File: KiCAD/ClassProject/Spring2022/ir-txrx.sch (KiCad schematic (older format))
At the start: 1 part

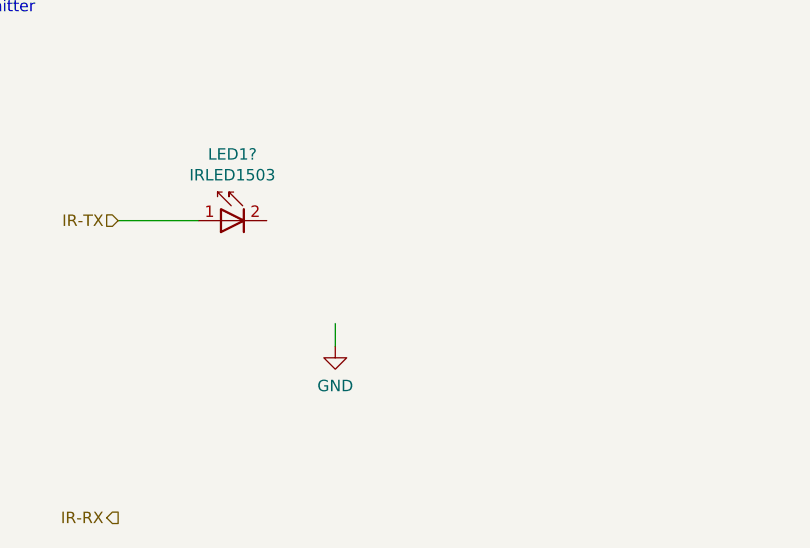
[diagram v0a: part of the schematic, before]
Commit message: Added decoupling caps and pull up resistors from PONTECH library
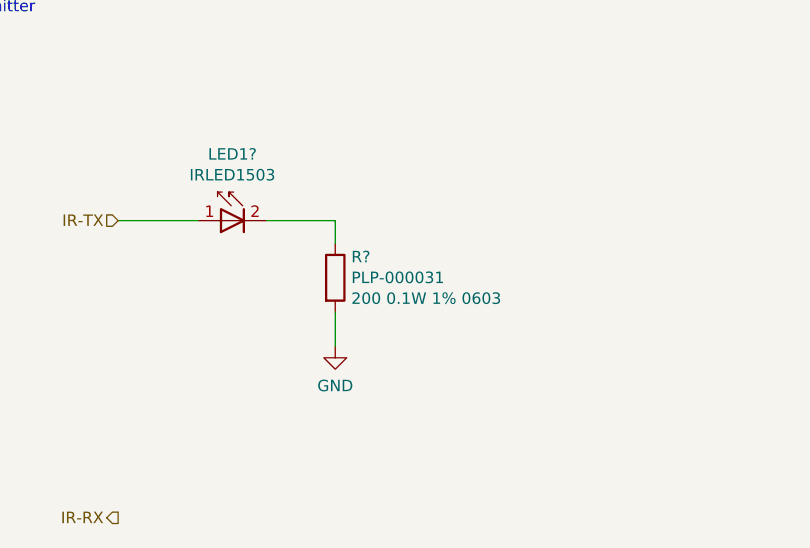
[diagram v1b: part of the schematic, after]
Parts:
- added R?: PLP-000031, a_pontech:R_0603_1608Metric, symbol 1_pontech:PLP-000031
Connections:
- wire segments 2 -> 4
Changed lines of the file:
@@
 Wire Wire Line
 	1900 2000 2250 2000
-Wire Wire Line
-	2850 2450 2850 2550
 $Comp
 L 74_Jacob:GND #PWR?
@@
 	1    0    0    -1
 $EndComp
+$Comp
+L 1_pontech:PLP-000031 R?
+U 1 1 62644FF5
+P 2850 2250
+F 0 "R?" H 2920 2341 50  0000 L CNN
+F 1 "PLP-000031" H 2920 2250 50  0000 L CNN
+F 2 "a_pontech:R_0603_1608Metric" V 2780 2250 50  0001 C CNN
+F 3 "~" H 2850 2250 50  0001 C CNN
+F 4 "200 0.1W 1% 0603" H 2920 2159 50  0000 L CNN "Info"
+	1    2850 2250
+	1    0    0    -1
+$EndComp
+Wire Wire Line
+	2850 2400 2850 2550
+Wire Wire Line
+	2850 2100 2850 2000
+Wire Wire Line
+	2850 2000 2550 2000
 $EndSCHEMATC

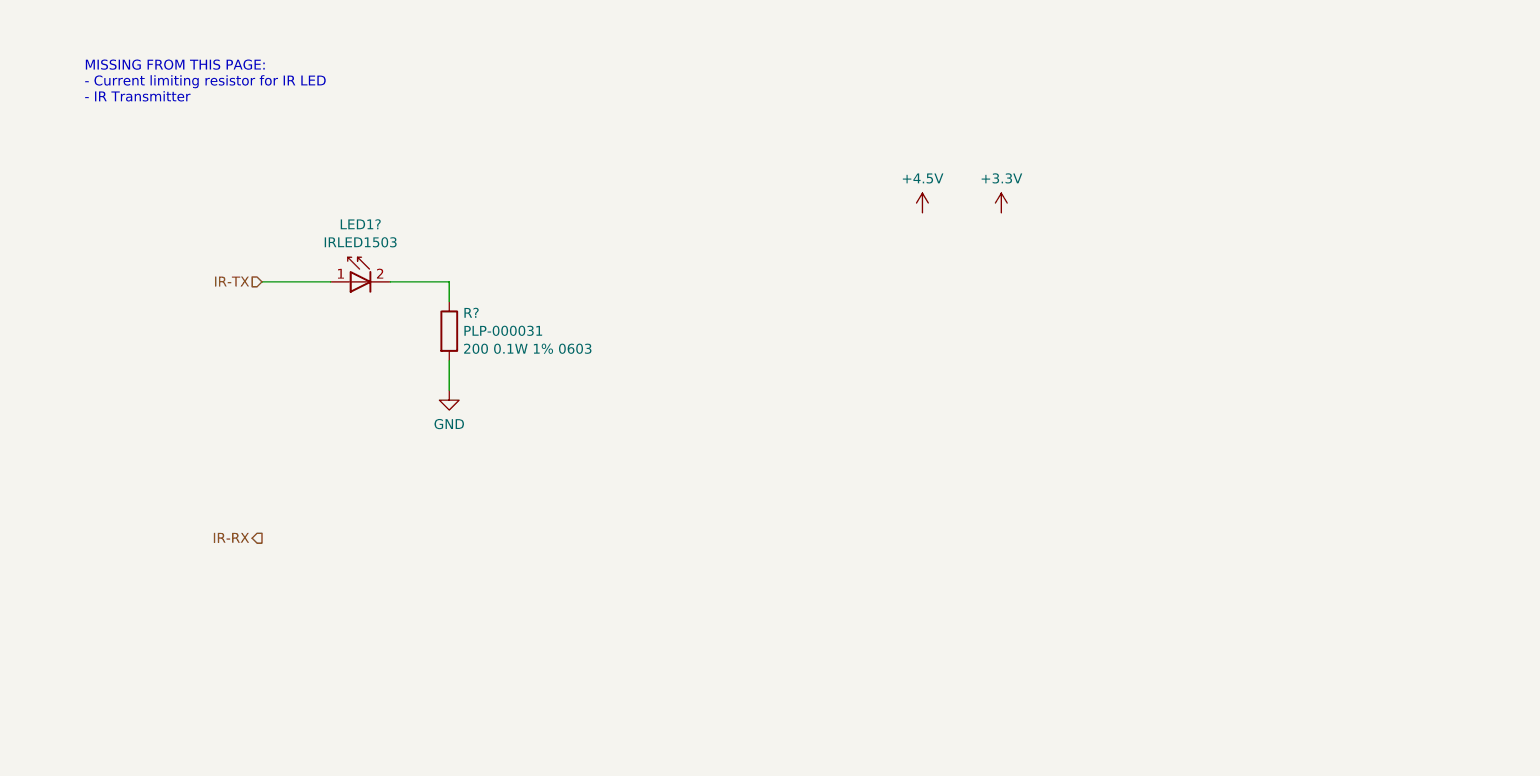
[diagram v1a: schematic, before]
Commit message: Added IR Tx
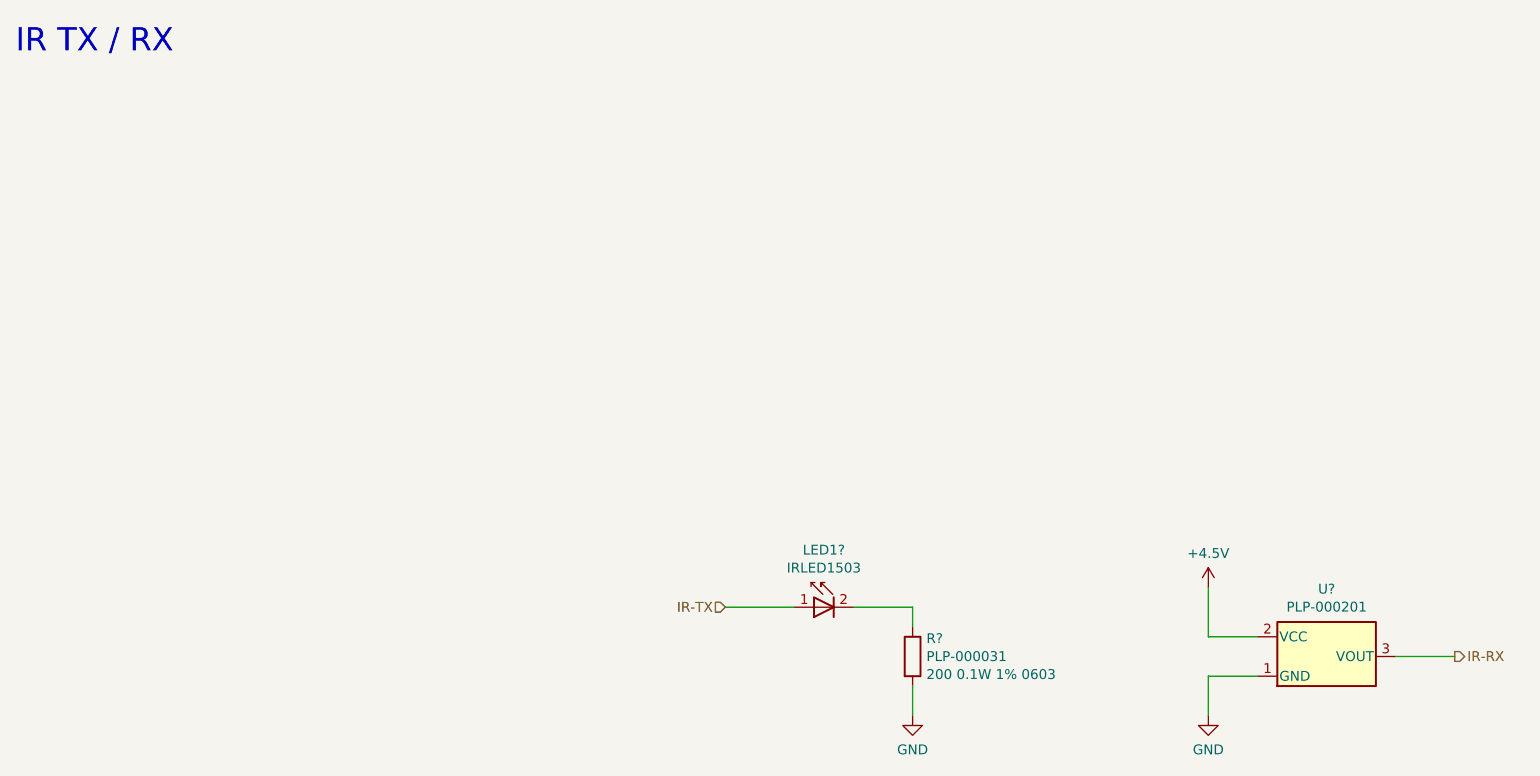
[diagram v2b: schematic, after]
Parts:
- added U?: PLP-000201, 1_pontech:PLP-0000201, symbol 1_pontech:PLP-000201
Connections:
- net +4V: now also U?.2 (VCC)
- net GND: now also U?.1 (GND)
- net IR-RX: now also U?.3 (VOUT)
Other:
- note added: "IR TX / RX"
- note removed: "MISSING FROM THIS PAGE:\n- Current limiting resistor for IR LED\n- IR Transmitter"
- moved on the sheet: LED1?, R?
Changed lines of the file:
@@
 L 74_Jordan_IRSchematic:IRLED1503 LED1?
 U 1 1 6265B928
-P 2400 2000
-F 0 "LED1?" H 2400 2290 50  0000 C CNN
-F 1 "IRLED1503" H 2400 2199 50  0000 C CNN
-F 2 "74_ClassProj_IRFootprint:IR1503" H 2400 1825 50  0001 C CNN
-F 3 "http://www.alliedelec.com/m/d/40788c34903a719969df15f1fbea1056.pdf" H 2750 1750 50  0001 C CNN
-	1    2400 2000
+P 4750 3650
+F 0 "LED1?" H 4750 3940 50  0000 C CNN
+F 1 "IRLED1503" H 4750 3849 50  0000 C CNN
+F 2 "74_ClassProj_IRFootprint:IR1503" H 4750 3475 50  0001 C CNN
+F 3 "http://www.alliedelec.com/m/d/40788c34903a719969df15f1fbea1056.pdf" H 5100 3400 50  0001 C CNN
+	1    4750 3650
 	-1   0    0    -1
 $EndComp
-Text Notes 1000 1100 0    50   ~ 0
-MISSING FROM THIS PAGE:\n- Current limiting resistor for IR LED\n- IR Transmitter
-Text HLabel 1900 2000 0    50   Input ~ 0
+Text HLabel 4250 3650 0    50   Input ~ 0
 IR-TX
-Text HLabel 1900 3300 0    50   Output ~ 0
+Text HLabel 7950 3900 2    50   Output ~ 0
 IR-RX
 Wire Wire Line
-	1900 2000 2250 2000
+	4250 3650 4600 3650
 $Comp
 L 74_Jacob:GND #PWR?
 U 1 1 6265D8F2
-P 2850 2550
+P 5200 4200
 AR Path="/6265D8F2" Ref="#PWR?"  Part="1"
 AR Path="/6265B89C/6265D8F2" Ref="#PWR?"  Part="1"
-F 0 "#PWR?" H 2850 2300 50  0001 C CNN
-F 1 "GND" H 2850 2377 50  0000 C CNN
-F 2 "" H 2850 2550 50  0001 C CNN
-F 3 "" H 2850 2550 50  0001 C CNN
-	1    2850 2550
+F 0 "#PWR?" H 5200 3950 50  0001 C CNN
+F 1 "GND" H 5200 4027 50  0000 C CNN
+F 2 "" H 5200 4200 50  0001 C CNN
+F 3 "" H 5200 4200 50  0001 C CNN
+	1    5200 4200
 	1    0    0    -1
 $EndComp
@@
 L 74_Jacob:+4.5V #PWR?
 U 1 1 626785BD
-P 5250 1650
-F 0 "#PWR?" H 5250 1500 50  0001 C CNN
-F 1 "+4.5V" H 5250 1823 50  0000 C CNN
-F 2 "" H 5250 1650 50  0001 C CNN
-F 3 "" H 5250 1650 50  0001 C CNN
-	1    5250 1650
-	1    0    0    -1
-$EndComp
-$Comp
-L 74_Jacob:+3.3V #PWR?
-U 1 1 62678C26
-P 5650 1650
-F 0 "#PWR?" H 5650 1500 50  0001 C CNN
-F 1 "+3.3V" H 5650 1823 50  0000 C CNN
-F 2 "" H 5650 1650 50  0001 C CNN
-F 3 "" H 5650 1650 50  0001 C CNN
-	1    5650 1650
+P 6700 3550
+F 0 "#PWR?" H 6700 3400 50  0001 C CNN
+F 1 "+4.5V" H 6700 3723 50  0000 C CNN
+F 2 "" H 6700 3550 50  0001 C CNN
+F 3 "" H 6700 3550 50  0001 C CNN
+	1    6700 3550
 	1    0    0    -1
 $EndComp
@@
 L 1_pontech:PLP-000031 R?
 U 1 1 62644FF5
-P 2850 2250
-F 0 "R?" H 2920 2341 50  0000 L CNN
-F 1 "PLP-000031" H 2920 2250 50  0000 L CNN
-F 2 "a_pontech:R_0603_1608Metric" V 2780 2250 50  0001 C CNN
-F 3 "~" H 2850 2250 50  0001 C CNN
-F 4 "200 0.1W 1% 0603" H 2920 2159 50  0000 L CNN "Info"
-	1    2850 2250
+P 5200 3900
+F 0 "R?" H 5270 3991 50  0000 L CNN
+F 1 "PLP-000031" H 5270 3900 50  0000 L CNN
+F 2 "a_pontech:R_0603_1608Metric" V 5130 3900 50  0001 C CNN
+F 3 "~" H 5200 3900 50  0001 C CNN
+F 4 "200 0.1W 1% 0603" H 5270 3809 50  0000 L CNN "Info"
+	1    5200 3900
 	1    0    0    -1
 $EndComp
 Wire Wire Line
-	2850 2400 2850 2550
+	5200 4050 5200 4200
 Wire Wire Line
-	2850 2100 2850 2000
+	5200 3750 5200 3650
 Wire Wire Line
-	2850 2000 2550 2000
+	5200 3650 4900 3650
+$Comp
+L 1_pontech:PLP-000201 U?
+U 1 1 62668197
+P 7300 3900
+F 0 "U?" H 7300 4242 50  0000 C CNN
+F 1 "PLP-000201" H 7300 4151 50  0000 C CNN
+F 2 "1_pontech:PLP-0000201" H 7300 4225 50  0001 C CIN
+F 3 "http://www.zlgmcu.com/Sipex/LDO/PDF/spx2920.pdf" H 7300 3950 50  0001 C CNN
+	1    7300 3900
+	1    0    0    -1
+$EndComp
+Wire Wire Line
+	7950 3900 7650 3900
+Wire Wire Line
+	6700 3550 6700 3800
+Wire Wire Line
+	6700 3800 6950 3800
+$Comp
+L 74_Jacob:GND #PWR?
+U 1 1 62669A75
+P 6700 4200
+AR Path="/62669A75" Ref="#PWR?"  Part="1"
+AR Path="/6265B89C/62669A75" Ref="#PWR?"  Part="1"
+F 0 "#PWR?" H 6700 3950 50  0001 C CNN
+F 1 "GND" H 6700 4027 50  0000 C CNN
+F 2 "" H 6700 4200 50  0001 C CNN
+F 3 "" H 6700 4200 50  0001 C CNN
+	1    6700 4200
+	1    0    0    -1
+$EndComp
+Wire Wire Line
+	6700 4200 6700 4000
+Wire Wire Line
+	6700 4000 6950 4000
+Text Notes 650  850  0    118  ~ 0
+IR TX / RX
 $EndSCHEMATC

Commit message: Nearly finished schematic and routing.
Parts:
- U8: renamed from U?; footprint 1_pontech:PLP-0000201 -> a_pontech:PLP-000201
- gave numbers to parts that had none: 2
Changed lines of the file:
@@
 $EndDescr
 $Comp
-L 74_Jordan_IRSchematic:IRLED1503 LED1?
+L 74_Jordan_IRSchematic:IRLED1503 LED11
 U 1 1 6265B928
 P 4750 3650
-F 0 "LED1?" H 4750 3940 50  0000 C CNN
+F 0 "LED11" H 4750 3940 50  0000 C CNN
 F 1 "IRLED1503" H 4750 3849 50  0000 C CNN
 F 2 "74_ClassProj_IRFootprint:IR1503" H 4750 3475 50  0001 C CNN
@@
 P 5200 4200
 AR Path="/6265D8F2" Ref="#PWR?"  Part="1"
-AR Path="/6265B89C/6265D8F2" Ref="#PWR?"  Part="1"
-F 0 "#PWR?" H 5200 3950 50  0001 C CNN
+AR Path="/6265B89C/6265D8F2" Ref="#PWR0118"  Part="1"
+F 0 "#PWR0118" H 5200 3950 50  0001 C CNN
 F 1 "GND" H 5200 4027 50  0000 C CNN
 F 2 "" H 5200 4200 50  0001 C CNN
@@
 $EndComp
 $Comp
-L 74_Jacob:+4.5V #PWR?
+L 74_Jacob:+4.5V #PWR0119
 U 1 1 626785BD
 P 6700 3550
-F 0 "#PWR?" H 6700 3400 50  0001 C CNN
+F 0 "#PWR0119" H 6700 3400 50  0001 C CNN
 F 1 "+4.5V" H 6700 3723 50  0000 C CNN
 F 2 "" H 6700 3550 50  0001 C CNN
@@
 $EndComp
 $Comp
-L 1_pontech:PLP-000031 R?
+L 1_pontech:PLP-000031 R19
 U 1 1 62644FF5
 P 5200 3900
-F 0 "R?" H 5270 3991 50  0000 L CNN
+F 0 "R19" H 5270 3991 50  0000 L CNN
 F 1 "PLP-000031" H 5270 3900 50  0000 L CNN
 F 2 "a_pontech:R_0603_1608Metric" V 5130 3900 50  0001 C CNN
@@
 	5200 3650 4900 3650
 $Comp
-L 1_pontech:PLP-000201 U?
+L 1_pontech:PLP-000201 U8
 U 1 1 62668197
 P 7300 3900
-F 0 "U?" H 7300 4242 50  0000 C CNN
+F 0 "U8" H 7300 4242 50  0000 C CNN
 F 1 "PLP-000201" H 7300 4151 50  0000 C CNN
-F 2 "1_pontech:PLP-0000201" H 7300 4225 50  0001 C CIN
+F 2 "a_pontech:PLP-000201" H 7300 4225 50  0001 C CIN
 F 3 "http://www.zlgmcu.com/Sipex/LDO/PDF/spx2920.pdf" H 7300 3950 50  0001 C CNN
 	1    7300 3900
@@
 P 6700 4200
 AR Path="/62669A75" Ref="#PWR?"  Part="1"
-AR Path="/6265B89C/62669A75" Ref="#PWR?"  Part="1"
-F 0 "#PWR?" H 6700 3950 50  0001 C CNN
+AR Path="/6265B89C/62669A75" Ref="#PWR0120"  Part="1"
+F 0 "#PWR0120" H 6700 3950 50  0001 C CNN
 F 1 "GND" H 6700 4027 50  0000 C CNN
 F 2 "" H 6700 4200 50  0001 C CNN
